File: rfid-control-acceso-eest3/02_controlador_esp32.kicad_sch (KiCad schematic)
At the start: 4 parts, among them J3 ESP32_S3_DEVKITC1_N16R8_44PIN, J4 ESP32_S3_DEVKITC1_N16R8_44PIN

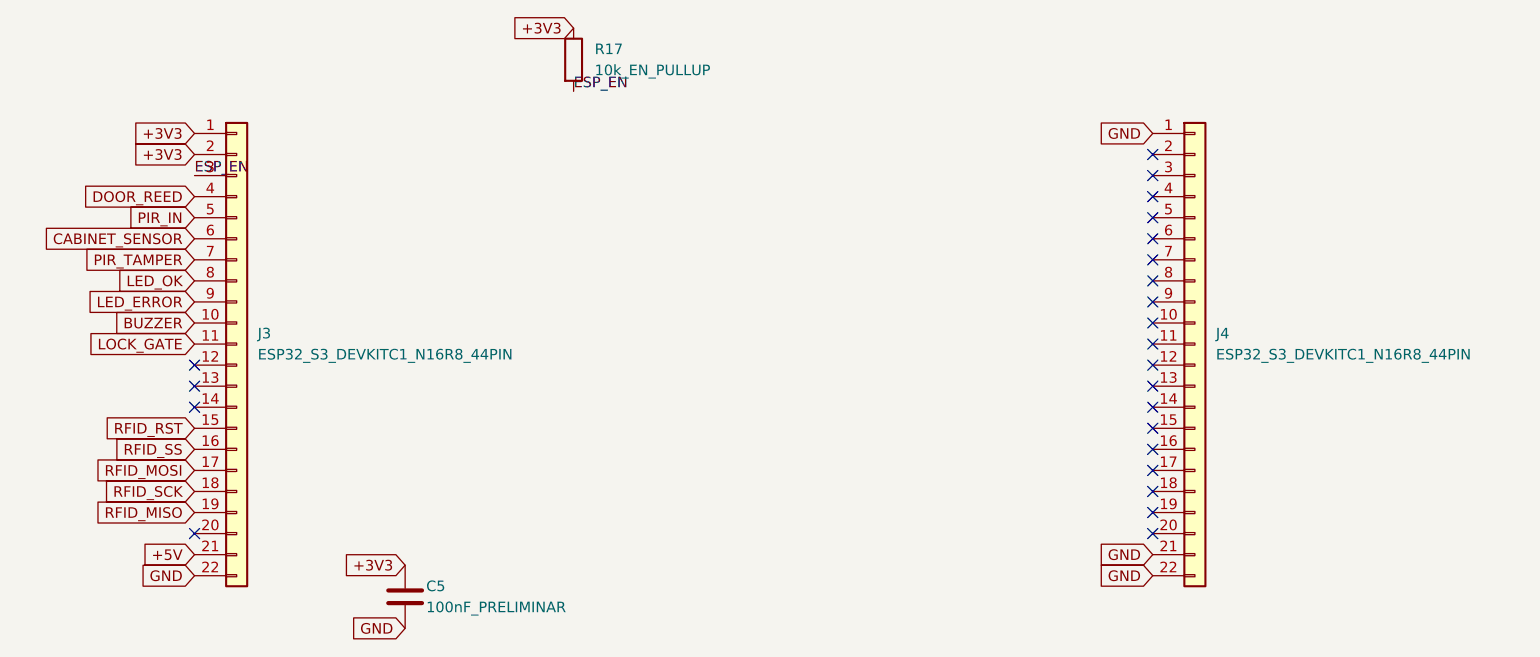
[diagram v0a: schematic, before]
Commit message: Reorganiza floorplan PCB Rev A antes del ruteo
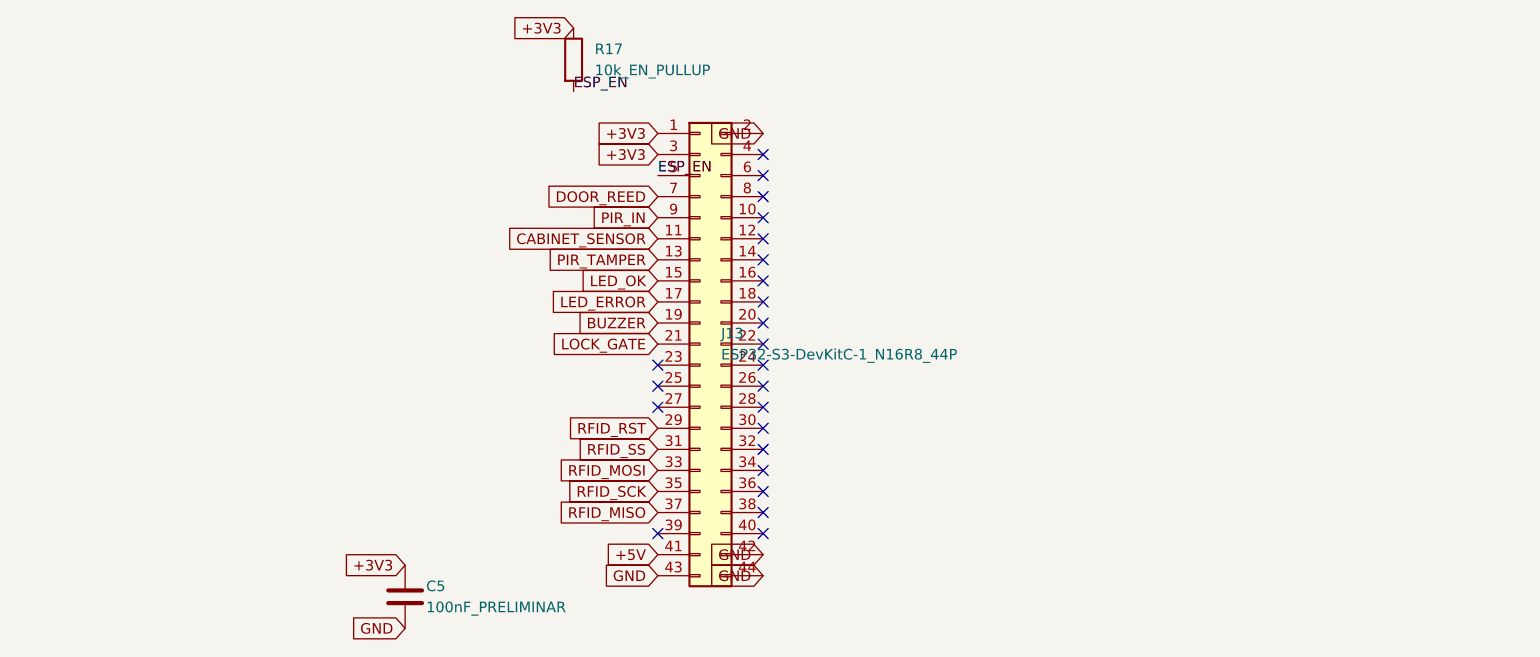
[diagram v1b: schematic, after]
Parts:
- removed J3, J4: ESP32_S3_DEVKITC1_N16R8_44PIN, symbol Connector_Generic:Conn_01x22
- added J13: ESP32-S3-DevKitC-1_N16R8_44P, rfid_eest3:ESP32-S3-DevKitC-1-44P_PLACEHOLDER_NO_FABRICAR, symbol Connector_Generic:Conn_02x22_Odd_Even
- C5: footprint (none) -> Capacitor_THT:C_Disc_D5.0mm_W2.5mm_P5.00mm
- R17: footprint (none) -> Resistor_THT:R_Axial_DIN0207_L6.3mm_D2.5mm_P10.16mm_Horizontal
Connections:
- net +3V3: now also J13.1 (Pin_1), J13.3 (Pin_3)
- net +5V: now also J13.41 (Pin_41)
- net BUZZER: now also J13.19 (Pin_19)
- net CABINET_SENSOR: now also J13.11 (Pin_11)
- net DOOR_REED: now also J13.7 (Pin_7)
- net ESP_EN: now also J13.5 (Pin_5)
- net GND: now also J13.2 (Pin_2), J13.42 (Pin_42), J13.43 (Pin_43), J13.44 (Pin_44)
- net LED_ERROR: now also J13.17 (Pin_17)
- net LED_OK: now also J13.15 (Pin_15)
- net LOCK_GATE: now also J13.21 (Pin_21)
- net PIR_IN: now also J13.9 (Pin_9)
- net PIR_TAMPER: now also J13.13 (Pin_13)
- net RFID_MISO: now also J13.37 (Pin_37)
- net RFID_MOSI: now also J13.33 (Pin_33)
- net RFID_RST: now also J13.29 (Pin_29)
- net RFID_SCK: now also J13.35 (Pin_35)
- net RFID_SS: now also J13.31 (Pin_31)
